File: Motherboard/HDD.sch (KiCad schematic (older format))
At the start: 6 parts, among them J1 SD_Card, U1 4081, U2 4001, U3 ATmega328-PU, U4 4081

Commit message: More work on Motherboard
Began work on PCB Routing
Began work on DMA
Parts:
- J1: footprint (none) -> Connectors:SD_Card_Receptacle
- RN1: footprint Resistor_THT:R_Array_SIP6 -> Resistors_THT:R_Array_SIP6
- U4: renamed from U1; footprint (none) -> Housings_DIP:DIP-14_W7.62mm_Socket
- U5: renamed from U2; footprint (none) -> Housings_LCC:PLCC-28_THT-Socket
- U6: renamed from U4; footprint (none) -> Housings_DIP:DIP-40_W15.24mm_Socket
- U7: renamed from U3; footprint Package_DIP:DIP-28_W7.62mm -> Housings_DIP:DIP-28_W15.24mm_Socket
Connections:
- net labels added: A2, A3, A4, A[0...19]
- net labels removed: ADDR, DATA
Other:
- moved on the sheet: U4E, U5E, U6E

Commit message: Added ISA Footprint
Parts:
- removed J1: SD_Card, Connectors:SD_Card_Receptacle, symbol Connector:SD_Card
- removed RN1: 50k, Resistors_THT:R_Array_SIP6, symbol Device:R_Network05
- added J1: SD_Connector, Connectors_Molex:Molex_KK-6410-06_06x2.54mm_Straight, symbol Connector_Generic:Conn_02x03_Counter_Clockwise
- U6: footprint Housings_DIP:DIP-40_W15.24mm_Socket -> Housings_DIP:DIP-14_W7.62mm_Socket
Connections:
- net labels added: MISO, MOSI, SCK, SS-CS
- wire segments 88 -> 76
- no-connect marks 4 -> 0
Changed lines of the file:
@@
 $Descr A4 11693 8268
 encoding utf-8
-Sheet 2 4
+Sheet 2 5
 Title ""
 Date ""
@@
 Text Label 9050 2575 2    50   ~ 0
 ~RESET
-$Comp
-L Connector:SD_Card J1
-U 1 1 5C0B390D
-P 6750 5100
-F 0 "J1" H 6750 4435 50  0000 C CNN
-F 1 "SD_Card" H 6750 4526 50  0000 C CNN
-F 2 "Connectors:SD_Card_Receptacle" H 6750 5100 50  0001 C CNN
-F 3 "http://portal.fciconnect.com/Comergent//fci/drawing/10067847.pdf" H 6750 5100 50  0001 C CNN
-	1    6750 5100
-	-1   0    0    1
-$EndComp
-Wire Wire Line
-	7650 5400 8850 5400
-Wire Wire Line
-	8850 5400 8850 4400
 Wire Wire Line
 	8850 3875 9100 3875
 Wire Wire Line
-	7650 5300 8750 5300
-Wire Wire Line
-	8750 5300 8750 3775
-Wire Wire Line
 	8750 3775 9100 3775
 Wire Wire Line
 	9100 3675 8650 3675
 Wire Wire Line
-	8650 4800 7650 4800
-Wire Wire Line
-	8650 3675 8650 4350
-Wire Wire Line
-	7650 5000 8550 5000
-Wire Wire Line
-	8550 5000 8550 4300
-Wire Wire Line
 	8550 3575 9100 3575
-$Comp
-L power:GND #PWR09
-U 1 1 5C0B5F56
-P 7650 5200
-F 0 "#PWR09" H 7650 4950 50  0001 C CNN
-F 1 "GND" V 7655 5072 50  0000 R CNN
-F 2 "" H 7650 5200 50  0001 C CNN
-F 3 "" H 7650 5200 50  0001 C CNN
-	1    7650 5200
-	0    -1   -1   0
-$EndComp
 $Comp
 L power:GND #PWR07
 U 1 1 5C0B5FAE
-P 7650 4900
-F 0 "#PWR07" H 7650 4650 50  0001 C CNN
-F 1 "GND" V 7655 4772 50  0000 R CNN
-F 2 "" H 7650 4900 50  0001 C CNN
-F 3 "" H 7650 4900 50  0001 C CNN
-	1    7650 4900
-	0    -1   -1   0
+P 7050 5425
+F 0 "#PWR07" H 7050 5175 50  0001 C CNN
+F 1 "GND" V 7055 5297 50  0000 R CNN
+F 2 "" H 7050 5425 50  0001 C CNN
+F 3 "" H 7050 5425 50  0001 C CNN
+	1    7050 5425
+	1    0    0    -1
 $EndComp
 $Comp
 L power:+5V #PWR08
 U 1 1 5C0B60D5
-P 7650 5100
-F 0 "#PWR08" H 7650 4950 50  0001 C CNN
-F 1 "+5V" V 7665 5228 50  0000 L CNN
-F 2 "" H 7650 5100 50  0001 C CNN
-F 3 "" H 7650 5100 50  0001 C CNN
-	1    7650 5100
-	0    1    1    0
-$EndComp
-$Comp
-L Device:R_Network05 RN1
-U 1 1 5C0B624F
-P 7950 4100
-F 0 "RN1" H 8230 4146 50  0000 L CNN
-F 1 "50k" H 8225 4075 50  0000 L CNN
-F 2 "Resistors_THT:R_Array_SIP6" V 8325 4100 50  0001 C CNN
-F 3 "http://www.vishay.com/docs/31509/csc.pdf" H 7950 4100 50  0001 C CNN
-	1    7950 4100
-	1    0    0    -1
-$EndComp
-Wire Wire Line
-	8150 4300 8550 4300
-Connection ~ 8550 4300
-Wire Wire Line
-	8550 4300 8550 3575
-Wire Wire Line
-	8050 4300 8050 4350
-Wire Wire Line
-	8050 4350 8650 4350
-Connection ~ 8650 4350
-Wire Wire Line
-	8650 4350 8650 4800
-Wire Wire Line
-	7950 4300 7950 4400
-Wire Wire Line
-	7950 4400 8850 4400
-Connection ~ 8850 4400
-Wire Wire Line
-	8850 4400 8850 3875
-Wire Wire Line
-	7975 5500 7975 4450
-Wire Wire Line
-	7975 4450 7850 4450
-Wire Wire Line
-	7850 4450 7850 4300
-Wire Wire Line
-	7650 5500 7975 5500
-Wire Wire Line
-	7650 4700 7750 4700
-Wire Wire Line
-	7750 4700 7750 4300
-$Comp
-L power:+5V #PWR010
-U 1 1 5C0B9DA2
-P 7750 3900
-F 0 "#PWR010" H 7750 3750 50  0001 C CNN
-F 1 "+5V" H 7765 4073 50  0000 C CNN
-F 2 "" H 7750 3900 50  0001 C CNN
-F 3 "" H 7750 3900 50  0001 C CNN
-	1    7750 3900
+P 7050 4925
+F 0 "#PWR08" H 7050 4775 50  0001 C CNN
+F 1 "+5V" V 7065 5053 50  0000 L CNN
+F 2 "" H 7050 4925 50  0001 C CNN
+F 3 "" H 7050 4925 50  0001 C CNN
+	1    7050 4925
 	1    0    0    -1
 $EndComp
@@
 F 0 "U6" H 2100 4275 50  0000 C CNN
 F 1 "4081" H 2100 4184 50  0000 C CNN
-F 2 "Housings_DIP:DIP-40_W15.24mm_Socket" H 2100 3950 50  0001 C CNN
+F 2 "Housings_DIP:DIP-14_W7.62mm_Socket" H 2100 3950 50  0001 C CNN
 F 3 "http://www.intersil.com/content/dam/Intersil/documents/cd40/cd4073bms-81bms-82bms.pdf" H 2100 3950 50  0001 C CNN
 	1    2100 3950
@@
 	2550 5975 3250 5975
 Connection ~ 2550 5975
-NoConn ~ 5850 4900
-NoConn ~ 5850 5000
-NoConn ~ 5850 5200
-NoConn ~ 5850 5300
 Wire Bus Line
 	1300 1675 1300 1850
@@
 Wire Wire Line
 	8950 2375 9100 2375
-Wire Bus Line
-	8850 1675 8850 2275
-Wire Bus Line
-	1300 1850 1300 4650
 Text Label 8950 1775 0    50   ~ 0
 A6
@@
 Text HLabel 1075 1850 0    50   BiDi ~ 0
 A[0...19]
+$Comp
+L Connector_Generic:Conn_02x03_Counter_Clockwise J1
+U 1 1 5C17F343
+P 7150 5125
+F 0 "J1" V 7154 5305 50  0000 L CNN
+F 1 "SD_Connector" V 7225 4425 50  0000 L CNN
+F 2 "Connectors_Molex:Molex_KK-6410-06_06x2.54mm_Straight" H 7150 5125 50  0001 C CNN
+F 3 "~" H 7150 5125 50  0001 C CNN
+	1    7150 5125
+	0    1    1    0
+$EndComp
+Wire Wire Line
+	8850 5550 7150 5550
+Wire Wire Line
+	7150 5550 7150 5425
+Wire Wire Line
+	8850 3875 8850 5550
+Text Label 7150 5550 0    50   ~ 0
+SS-CS
+Wire Wire Line
+	7250 5425 8750 5425
+Wire Wire Line
+	8750 3775 8750 5425
+Text Label 7250 5425 0    50   ~ 0
+MOSI
+Wire Wire Line
+	7250 4925 8650 4925
+Wire Wire Line
+	8650 3675 8650 4925
+Wire Wire Line
+	8550 3575 8550 4825
+Wire Wire Line
+	8550 4825 7150 4825
+Wire Wire Line
+	7150 4825 7150 4925
+Wire Bus Line
+	8850 1675 8850 2275
+Wire Bus Line
+	1300 1850 1300 4650
+Text Label 7250 4925 0    50   ~ 0
+MISO
+Text Label 7150 4825 0    50   ~ 0
+SCK
 $EndSCHEMATC

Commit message: Large sync
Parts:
- added U39: ATF750LVC, Housings_DIP:DIP-28_W7.62mm_Socket, symbol fdc:ATF750LVC
- U6: footprint Housings_DIP:DIP-40_W15.24mm_Socket -> Housings_DIP:DIP-14_W7.62mm_Socket
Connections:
- net labels added: ADDR, D0, D1, D2, D3, D4, D5, D6, D7, D[0...7]
- net labels removed: A2, A3, A4
- wire segments 76 -> 100
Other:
- note added: "ADDR=A19*A18*~(A17+A16)~*~(A15+A14)~*A13*A9*A8*~(A7+A6)~*A5"
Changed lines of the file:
@@
 F 0 "U6" H 2700 4550 50  0000 C CNN
 F 1 "4081" H 2700 4459 50  0000 C CNN
-F 2 "Housings_DIP:DIP-40_W15.24mm_Socket" H 2700 4225 50  0001 C CNN
+F 2 "Housings_DIP:DIP-14_W7.62mm_Socket" H 2700 4225 50  0001 C CNN
 F 3 "http://www.intersil.com/content/dam/Intersil/documents/cd40/cd4073bms-81bms-82bms.pdf" H 2700 4225 50  0001 C CNN
 	2    2700 4225
@@
 F 0 "U6" H 3300 4925 50  0000 C CNN
 F 1 "4081" H 3300 4834 50  0000 C CNN
-F 2 "Housings_DIP:DIP-40_W15.24mm_Socket" H 3300 4600 50  0001 C CNN
+F 2 "Housings_DIP:DIP-14_W7.62mm_Socket" H 3300 4600 50  0001 C CNN
 F 3 "http://www.intersil.com/content/dam/Intersil/documents/cd40/cd4073bms-81bms-82bms.pdf" H 3300 4600 50  0001 C CNN
 	3    3300 4600
@@
 F 0 "U6" H 2780 6521 50  0000 L CNN
 F 1 "4081" H 2780 6430 50  0000 L CNN
-F 2 "Housings_DIP:DIP-40_W15.24mm_Socket" H 2550 6475 50  0001 C CNN
+F 2 "Housings_DIP:DIP-14_W7.62mm_Socket" H 2550 6475 50  0001 C CNN
 F 3 "http://www.intersil.com/content/dam/Intersil/documents/cd40/cd4073bms-81bms-82bms.pdf" H 2550 6475 50  0001 C CNN
 	5    2550 6475
@@
 A1
 Text Label 9050 2875 2    50   ~ 0
-ADDR_LO
-Text Label 9050 2975 2    50   ~ 0
-ADDR_HI
+ADDR
 Wire Wire Line
 	9100 3075 9050 3075
@@
 	2550 5975 3250 5975
 Connection ~ 2550 5975
-Wire Bus Line
-	1300 1675 1300 1850
-Connection ~ 1300 1850
-Wire Bus Line
-	8850 1575 8850 1675
-Connection ~ 8850 1675
 Wire Wire Line
 	2125 6975 2550 6975
@@
 	2550 6975 3250 6975
 Text Label 8950 1675 0    50   ~ 0
-A7
-Wire Bus Line
-	1300 1675 8850 1675
+D7
 Wire Wire Line
 	8950 1675 9100 1675
@@
 	8950 2375 9100 2375
 Text Label 8950 1775 0    50   ~ 0
-A6
+D6
 Text Label 8950 1875 0    50   ~ 0
-A5
+D5
 Text Label 8950 1975 0    50   ~ 0
-A4
+D4
 Text Label 8950 2075 0    50   ~ 0
-A3
+D3
 Text Label 8950 2175 0    50   ~ 0
-A2
+D2
 Text Label 8950 2275 0    50   ~ 0
-A1
+D1
 Text Label 8950 2375 0    50   ~ 0
-A0
+D0
 Text HLabel 1075 1850 0    50   BiDi ~ 0
 A[0...19]
@@
 Text Label 7150 4825 0    50   ~ 0
 SCK
+$Comp
+L fdc:ATF750LVC U39
+U 1 1 5C45A3F7
+P 5900 3450
+F 0 "U39" H 5900 4317 50  0000 C CNN
+F 1 "ATF750LVC" H 5900 4226 50  0000 C CNN
+F 2 "Housings_DIP:DIP-28_W7.62mm_Socket" H 5900 3450 50  0001 L CNN
+F 3 "" H 5900 3450 50  0001 L CNN
+	1    5900 3450
+	1    0    0    -1
+$EndComp
+Wire Wire Line
+	5400 2850 5175 2850
+Wire Wire Line
+	5400 2950 5175 2950
+Wire Wire Line
+	5175 3050 5400 3050
+Wire Wire Line
+	5400 3150 5175 3150
+Wire Wire Line
+	5400 3250 5175 3250
+Wire Wire Line
+	5175 3350 5400 3350
+Wire Wire Line
+	5400 3450 5175 3450
+Wire Wire Line
+	5400 3550 5175 3550
+Wire Wire Line
+	5175 3650 5400 3650
+Wire Wire Line
+	5400 3750 5175 3750
+Wire Wire Line
+	5400 3850 5175 3850
+Wire Wire Line
+	5175 3950 5400 3950
+Wire Wire Line
+	6625 2850 6400 2850
+Wire Wire Line
+	6625 2950 6400 2950
+Wire Wire Line
+	6400 3050 6625 3050
+Wire Wire Line
+	6625 3150 6400 3150
+Wire Wire Line
+	6625 3250 6400 3250
+Wire Wire Line
+	6400 3350 6625 3350
+Wire Wire Line
+	6625 3450 6400 3450
+Wire Wire Line
+	6625 3550 6400 3550
+Wire Wire Line
+	6400 3650 6625 3650
+Wire Wire Line
+	6625 3750 6400 3750
+Wire Wire Line
+	6625 3850 6400 3850
+Wire Wire Line
+	6400 3950 6625 3950
+Text Label 5175 2850 0    50   ~ 0
+A19
+Text Label 5175 2950 0    50   ~ 0
+A18
+Text Label 5175 3050 0    50   ~ 0
+A17
+Text Label 5175 3150 0    50   ~ 0
+A16
+Text Label 5175 3250 0    50   ~ 0
+A15
+Text Label 5175 3350 0    50   ~ 0
+A14
+Text Label 5175 3450 0    50   ~ 0
+A13
+Text Label 5175 3550 0    50   ~ 0
+A9
+Text Label 5175 3650 0    50   ~ 0
+A8
+Text Label 5175 3750 0    50   ~ 0
+A7
+Text Label 5175 3850 0    50   ~ 0
+A6
+Text Label 6625 3950 2    50   ~ 0
+A5
+$Comp
+L power:GND #PWR09
+U 1 1 5C46903C
+P 5175 3950
+F 0 "#PWR09" H 5175 3700 50  0001 C CNN
+F 1 "GND" H 5180 3777 50  0000 C CNN
+F 2 "" H 5175 3950 50  0001 C CNN
+F 3 "" H 5175 3950 50  0001 C CNN
+	1    5175 3950
+	1    0    0    -1
+$EndComp
+$Comp
+L power:+5V #PWR010
+U 1 1 5C469186
+P 6625 2850
+F 0 "#PWR010" H 6625 2700 50  0001 C CNN
+F 1 "+5V" H 6640 3023 50  0000 C CNN
+F 2 "" H 6625 2850 50  0001 C CNN
+F 3 "" H 6625 2850 50  0001 C CNN
+	1    6625 2850
+	1    0    0    -1
+$EndComp
+Text Label 6625 2950 2    50   ~ 0
+ADDR
 Wire Bus Line
-	8850 1675 8850 2275
+	8850 1350 8850 2275
 Wire Bus Line
 	1300 1850 1300 4650
+Text HLabel 8850 1350 1    50   BiDi ~ 0
+D[0...7]
+Text Notes 4700 2500 0    50   ~ 0
+ADDR=A19*A18*~(A17+A16)~*~(A15+A14)~*A13*A9*A8*~(A7+A6)~*A5
 $EndSCHEMATC

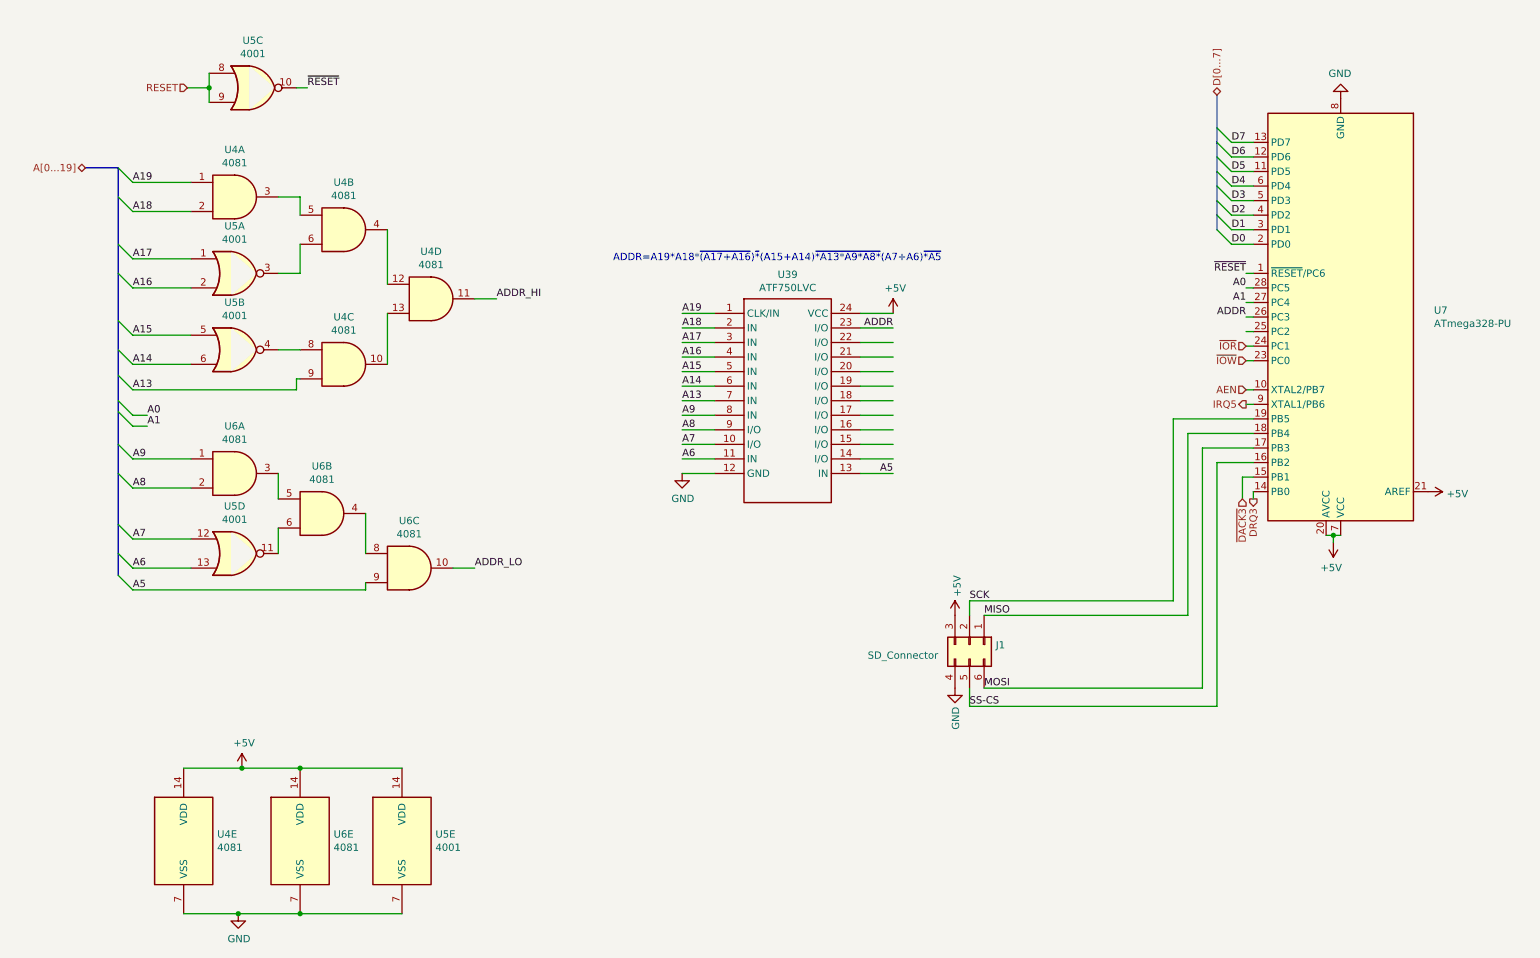
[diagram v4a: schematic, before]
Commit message: Work on motherboard  - Integrating glue logic into CPLD  - Began work on routing
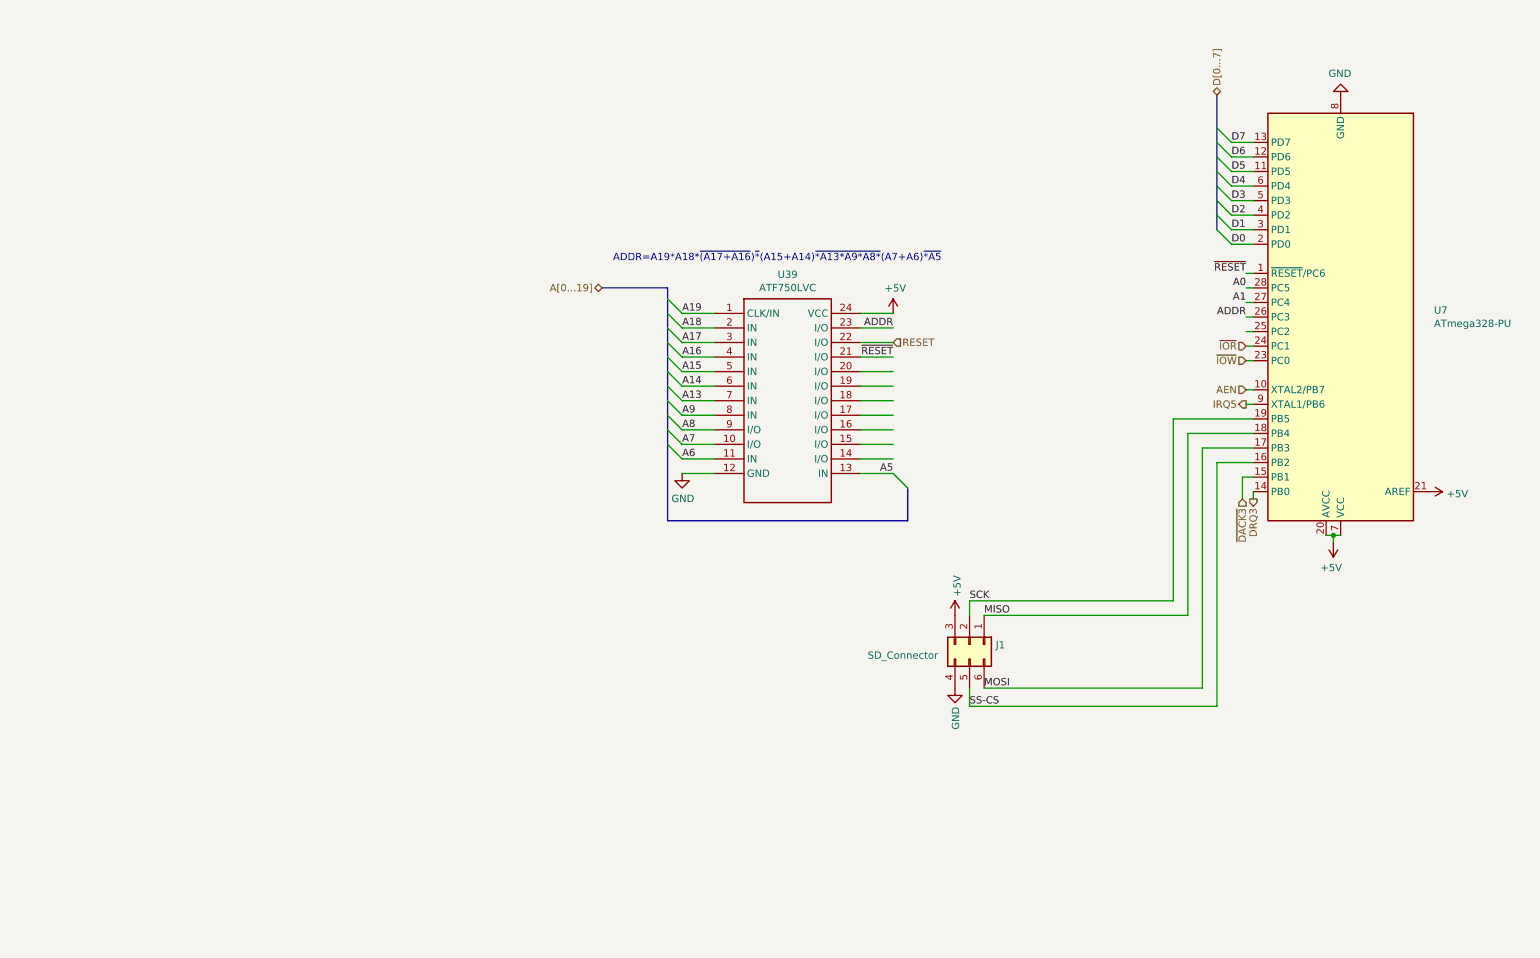
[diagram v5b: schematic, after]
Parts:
- removed U4, U6: 4081, Housings_DIP:DIP-14_W7.62mm_Socket, symbol 4xxx:4081
- removed U5: 4001, Housings_LCC:PLCC-28_THT-Socket, symbol 4xxx:4001
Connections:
- net labels removed: ADDR_HI, ADDR_LO
- wire segments 100 -> 61

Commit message: Large sync
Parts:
- U39: symbol fdc:ATF750LVC -> Motherboard-rescue:ATF750LVC-fdc
- U7: footprint Housings_DIP:DIP-28_W15.24mm_Socket -> Housings_DIP:DIP-28_W7.62mm_Socket
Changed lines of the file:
@@
 $Descr A4 11693 8268
 encoding utf-8
-Sheet 2 8
+Sheet 2 10
 Title ""
 Date ""
@@
 F 0 "U7" H 9059 2829 50  0000 R CNN
 F 1 "ATmega328-PU" H 9059 2920 50  0000 R CNN
-F 2 "Housings_DIP:DIP-28_W15.24mm_Socket" H 9700 2875 50  0001 C CIN
+F 2 "Housings_DIP:DIP-28_W7.62mm_Socket" H 9700 2875 50  0001 C CIN
 F 3 "http://ww1.microchip.com/downloads/en/DeviceDoc/ATmega328_P%20AVR%20MCU%20with%20picoPower%20Technology%20Data%20Sheet%2040001984A.pdf" H 9700 2875 50  0001 C CNN
 	1    9700 2875
@@
 Text Label 9050 2675 2    50   ~ 0
 A0
-Wire Wire Line
-	9100 2675 9050 2675
-Wire Wire Line
-	9050 2775 9100 2775
 Wire Wire Line
 	9100 2875 9050 2875
@@
 SCK
 $Comp
-L fdc:ATF750LVC U39
+L Motherboard-rescue:ATF750LVC-fdc U39
 U 1 1 5C45A3F7
 P 5900 3450
@@
 	4625 2675 5075 2675
 Wire Bus Line
+	6725 4275 7750 4275
+Wire Bus Line
+	7750 4275 7750 2525
+Wire Bus Line
+	7750 2525 8675 2525
+Connection ~ 6725 4275
+Entry Wire Line
+	8675 2675 8775 2775
+Entry Wire Line
+	8675 2575 8775 2675
+Wire Wire Line
+	8775 2675 9100 2675
+Wire Wire Line
+	8775 2775 9100 2775
+Wire Bus Line
+	8675 2525 8675 2675
+Wire Bus Line
 	8850 1350 8850 2275
